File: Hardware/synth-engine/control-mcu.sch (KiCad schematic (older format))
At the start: 31 parts

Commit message: add 3.3V analog regulator and add power nets to AK4490
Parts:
- removed J?: SWD_programming, symbol Connector:Conn_01x05_Male
- removed J? (x2): MIDI IN, symbol Connector:Conn_01x02_Female
- added C? (x7): C_Small, symbol Device:C_Small
- added J?: MIDI_IN, symbol Connector_Generic:Conn_01x02
- added J?: MIDI_OUT, symbol Connector_Generic:Conn_01x02
- added J?: SWD_programming, symbol Connector_Generic:Conn_01x05
- added R? (x14): 0, symbol Device:R
- added RV? (x7): 20kB, symbol Device:R_POT
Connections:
- net labels added: 3.3V, GND, attack, decay, lfo_depth, lfo_rate, release, sustain, waveshape
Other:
- note added: "Envelope Control Pots (ADSR)"
- note added: "LFO"
- note added: "MIDI"
- note added: "Waveshape"
- moved on the sheet: D?, Q?, R?, U?

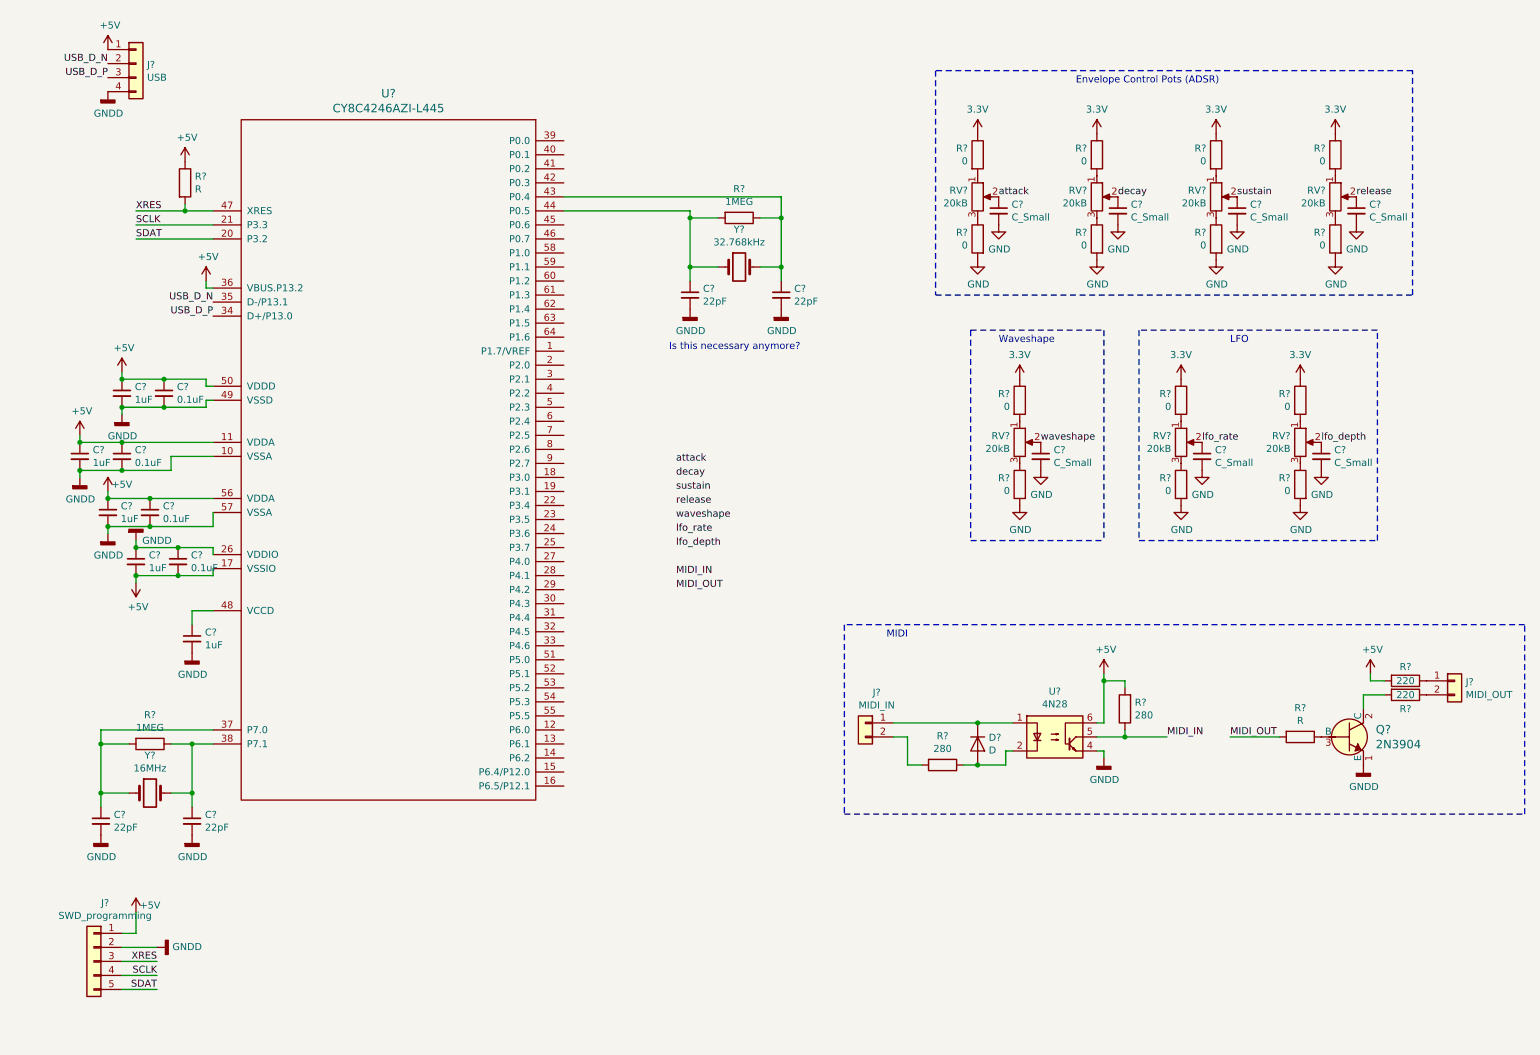
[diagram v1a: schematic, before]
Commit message: add potentiometers for 2 oscillators * I Think this will be all I need for potentiometers   * Until I think of something else to add, of course. * Waveshape will be a continuous change through all of the waves * Tune will be a center frequency control   * Basically just an offset away from the MIDI note's frequency
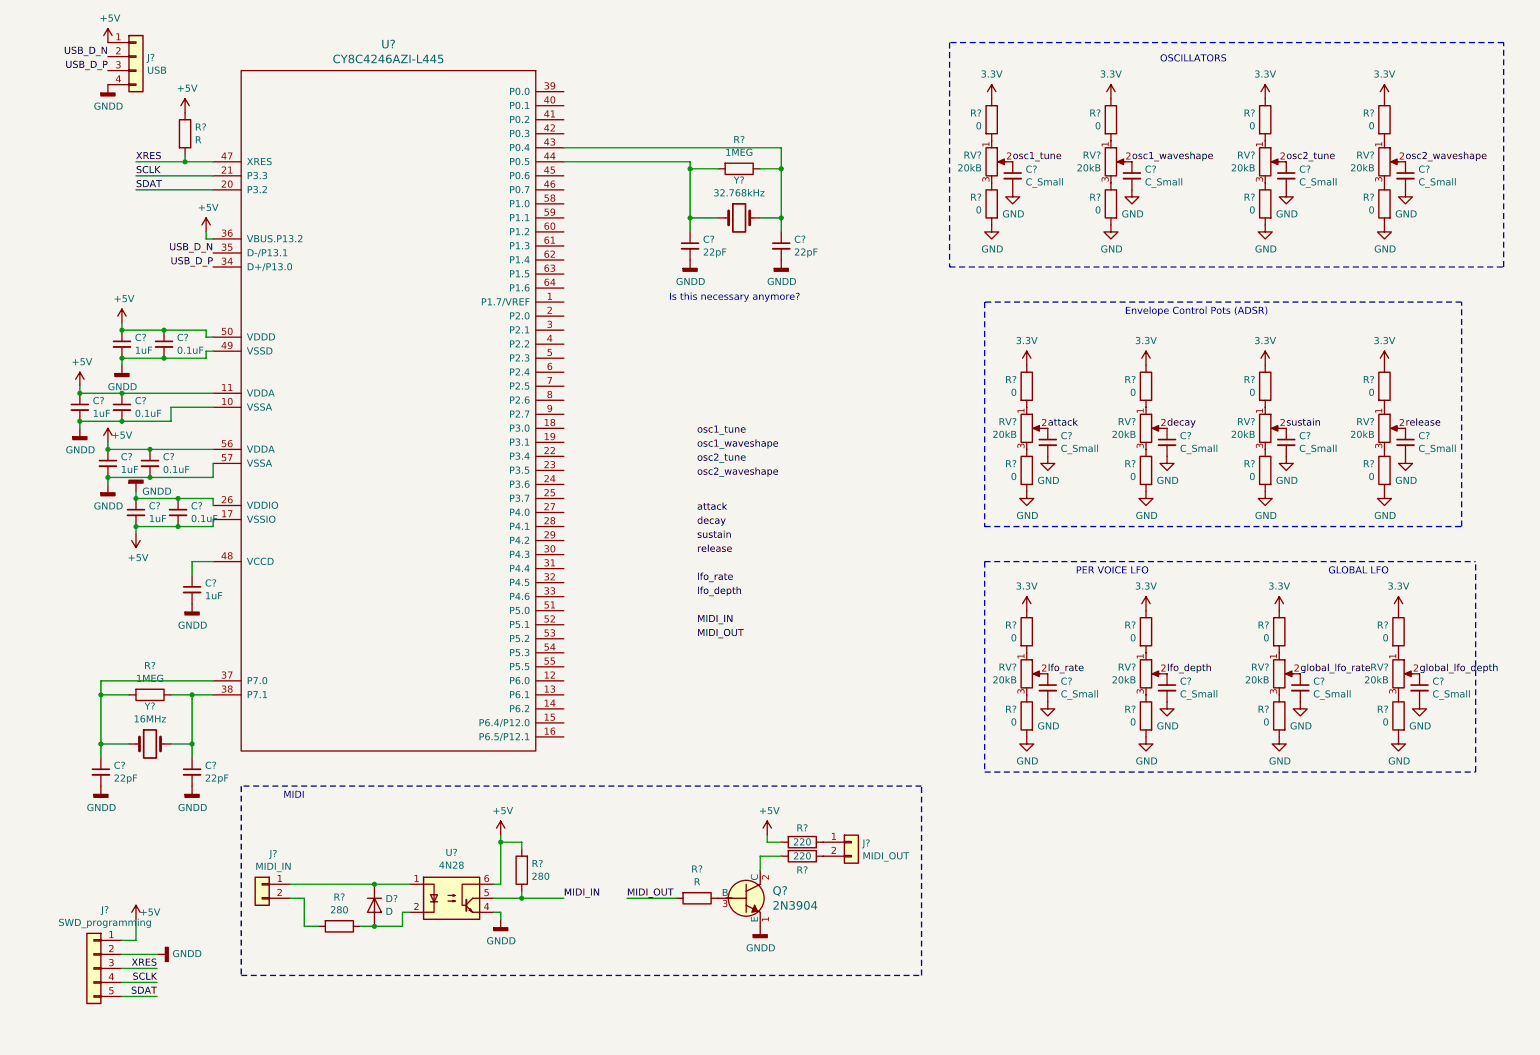
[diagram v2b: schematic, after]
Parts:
- added C? (x5): C_Small, symbol Device:C_Small
- added R? (x10): 0, symbol Device:R
- added RV? (x5): 20kB, symbol Device:R_POT
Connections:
- net 3.3V: now also R?.1, R?.1, R?.1, R?.1, R?.1
- net GND: now also C?.2, C?.2, C?.2, C?.2, C?.2, R?.2, R?.2, R?.2, R?.2, R?.2
- net lfo_depth: now also C?.1, RV?.2; no longer C?.1, RV?.2
- net lfo_rate: now also C?.1, RV?.2; no longer C?.1, RV?.2
- net waveshape renamed osc1_tune
- new net: R?.2, RV?.1 (x5)
- new net: R?.1, RV?.3 (x5)
- new net global_lfo_depth: C?.1, RV?.2
- new net global_lfo_rate: C?.1, RV?.2
- new net osc1_waveshape: C?.1, RV?.2
- new net osc2_tune: C?.1, RV?.2
- new net osc2_waveshape: C?.1, RV?.2
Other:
- note added: "GLOBAL LFO"
- note added: "OSCILLATORS"
- note added: "PER VOICE LFO"
- note removed: "LFO"
- note removed: "Waveshape"
- moved on the sheet: C?, D?, J?, Q?, R?, RV?, U?, Y?

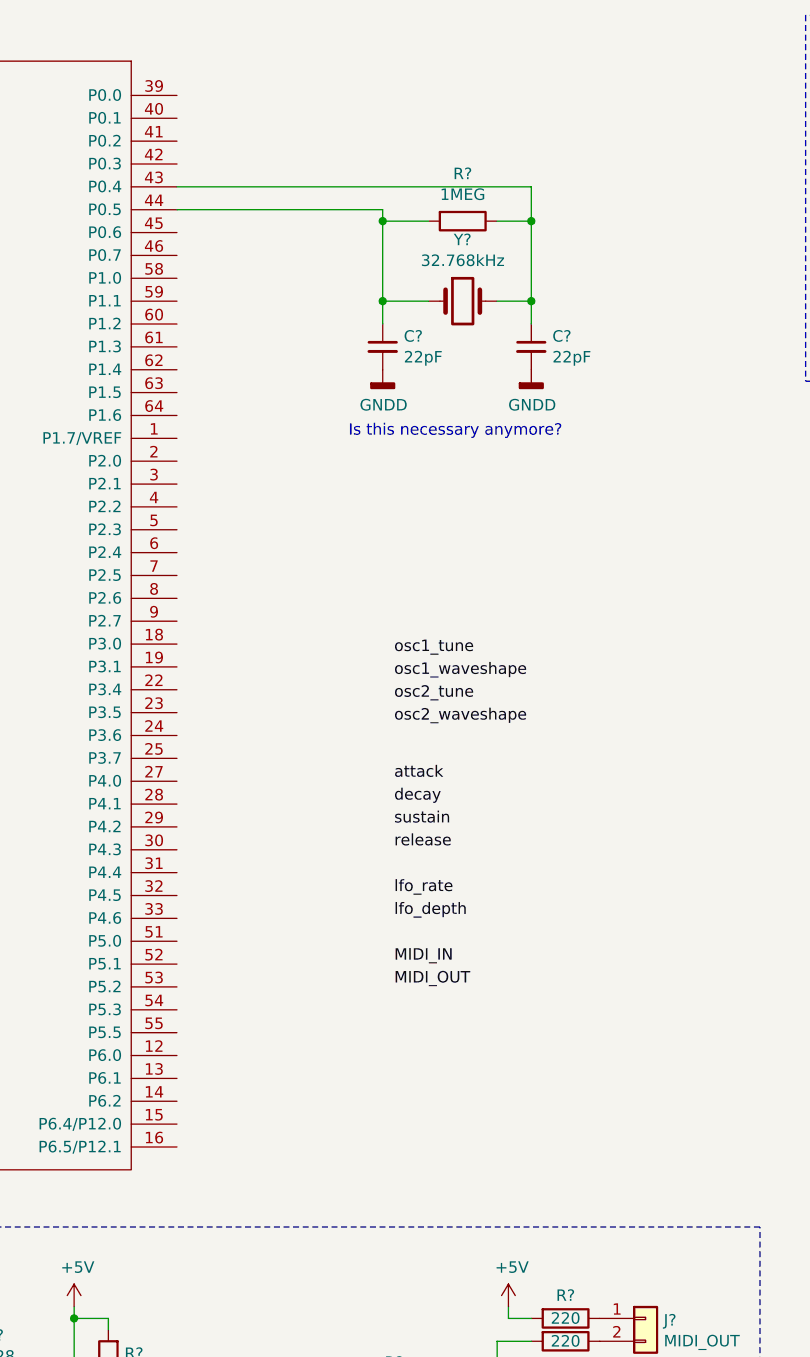
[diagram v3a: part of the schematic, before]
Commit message: delete low frequency crystal on PSoC schematic
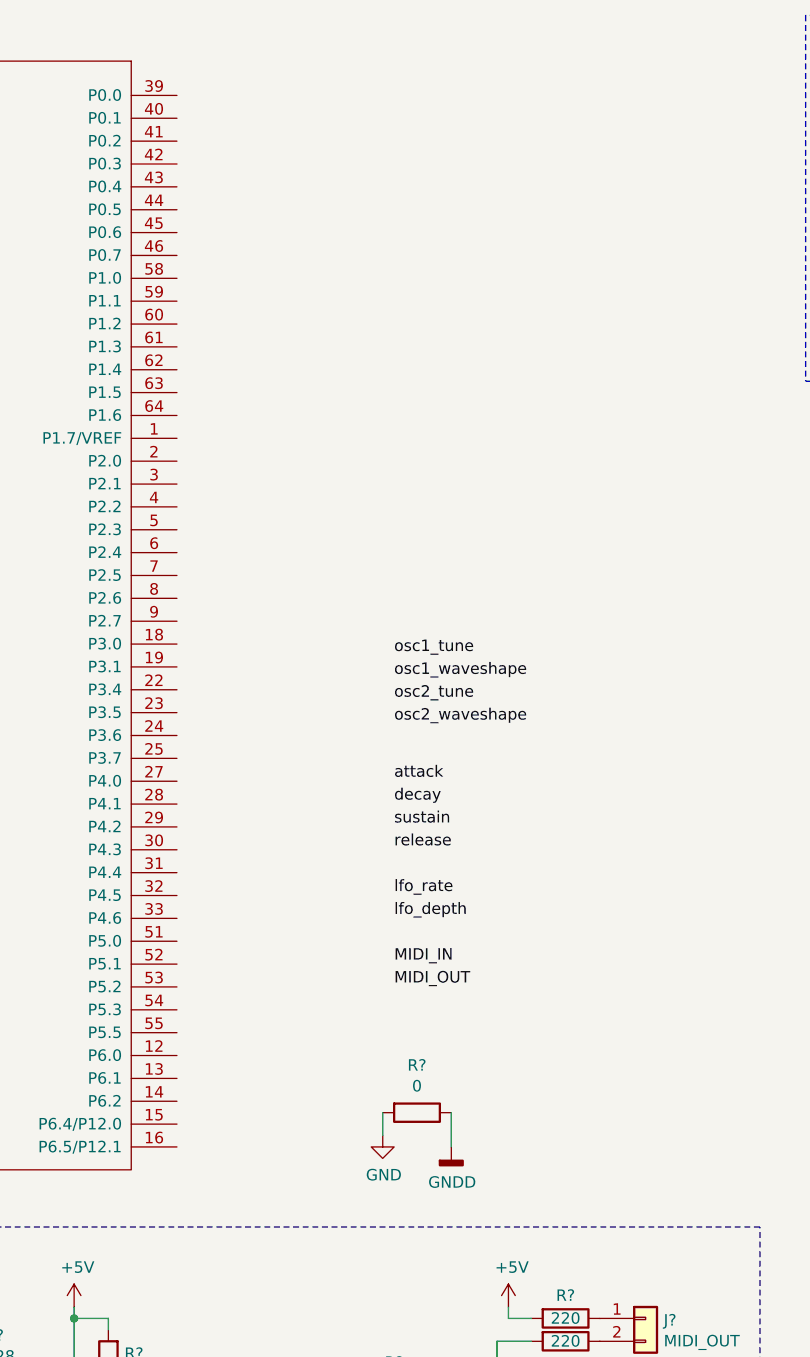
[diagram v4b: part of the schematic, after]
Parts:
- removed C? (x2): 22pF, symbol Device:C_Small
- removed R?: 1MEG, symbol Device:R
- removed Y?: 32.768kHz, symbol Device:Crystal
- added R?: 0, symbol Device:R
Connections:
- net GND: now also R?.2
- net GNDD: now also R?.1
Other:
- note removed: "Is this necessary anymore?"
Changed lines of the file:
@@
 Text Label 5050 3850 0    50   ~ 0
 osc2_waveshape
-Text Notes 4850 2600 0    50   ~ 0
-Is this necessary anymore?
-Wire Wire Line
-	4100 1600 5000 1600
-Wire Wire Line
-	4100 1500 5650 1500
-Wire Wire Line
-	5000 2000 5000 2100
-Connection ~ 5000 2000
-Wire Wire Line
-	5200 2000 5000 2000
 $Comp
-L power:GNDD #PWR?
-U 1 1 5DDBF7A4
-P 5650 2300
-F 0 "#PWR?" H 5650 2050 50  0001 C CNN
-F 1 "GNDD" H 5654 2145 50  0000 C CNN
-F 2 "" H 5650 2300 50  0001 C CNN
-F 3 "" H 5650 2300 50  0001 C CNN
-	1    5650 2300
-	1    0    0    -1
-$EndComp
-$Comp
-L power:GNDD #PWR?
-U 1 1 5DDBF79E
-P 5000 2300
-F 0 "#PWR?" H 5000 2050 50  0001 C CNN
-F 1 "GNDD" H 5004 2145 50  0000 C CNN
-F 2 "" H 5000 2300 50  0001 C CNN
-F 3 "" H 5000 2300 50  0001 C CNN
-	1    5000 2300
-	1    0    0    -1
-$EndComp
-Wire Wire Line
-	5000 1600 5000 1650
-Wire Wire Line
-	5000 1650 5000 2000
-Connection ~ 5000 1650
-Wire Wire Line
-	5200 1650 5000 1650
-Wire Wire Line
-	5500 2000 5650 2000
-Wire Wire Line
-	5650 1500 5650 1650
-Wire Wire Line
-	5650 2000 5650 1650
-Connection ~ 5650 1650
-Wire Wire Line
-	5650 1650 5500 1650
-Connection ~ 5650 2000
-Wire Wire Line
-	5650 2100 5650 2000
-$Comp
-L Device:Crystal Y?
-U 1 1 5DDBF790
-P 5350 2000
-F 0 "Y?" H 5350 2268 50  0000 C CNN
-F 1 "32.768kHz" H 5350 2177 50  0000 C CNN
-F 2 "" H 5350 2000 50  0001 C CNN
-F 3 "~" H 5350 2000 50  0001 C CNN
-	1    5350 2000
-	1    0    0    -1
-$EndComp
-$Comp
-L Device:C_Small C?
-U 1 1 5DDBF789
-P 5650 2200
-F 0 "C?" H 5742 2246 50  0000 L CNN
-F 1 "22pF" H 5742 2155 50  0000 L CNN
-F 2 "" H 5650 2200 50  0001 C CNN
-F 3 "~" H 5650 2200 50  0001 C CNN
-	1    5650 2200
-	1    0    0    -1
-$EndComp
-$Comp
-L Device:C_Small C?
-U 1 1 5DDBF782
-P 5000 2200
-F 0 "C?" H 5092 2246 50  0000 L CNN
-F 1 "22pF" H 5092 2155 50  0000 L CNN
-F 2 "" H 5000 2200 50  0001 C CNN
-F 3 "~" H 5000 2200 50  0001 C CNN
-	1    5000 2200
+L power:GND #PWR?
+U 1 1 5DD70135
+P 5000 5650
+F 0 "#PWR?" H 5000 5400 50  0001 C CNN
+F 1 "GND" H 5005 5477 50  0000 C CNN
+F 2 "" H 5000 5650 50  0001 C CNN
+F 3 "" H 5000 5650 50  0001 C CNN
+	1    5000 5650
 	1    0    0    -1
 $EndComp
 $Comp
 L Device:R R?
-U 1 1 5DDBF77B
-P 5350 1650
-F 0 "R?" V 5143 1650 50  0000 C CNN
-F 1 "1MEG" V 5234 1650 50  0000 C CNN
-F 2 "" V 5280 1650 50  0001 C CNN
-F 3 "~" H 5350 1650 50  0001 C CNN
-	1    5350 1650
+U 1 1 5DD70259
+P 5150 5550
+F 0 "R?" V 4943 5550 50  0000 C CNN
+F 1 "0" V 5034 5550 50  0000 C CNN
+F 2 "" V 5080 5550 50  0001 C CNN
+F 3 "~" H 5150 5550 50  0001 C CNN
+	1    5150 5550
 	0    1    1    0
 $EndComp
+Wire Wire Line
+	5000 5550 5000 5650
+$Comp
+L power:GNDD #PWR?
+U 1 1 5DD74B76
+P 5300 5700
+F 0 "#PWR?" H 5300 5450 50  0001 C CNN
+F 1 "GNDD" H 5304 5545 50  0000 C CNN
+F 2 "" H 5300 5700 50  0001 C CNN
+F 3 "" H 5300 5700 50  0001 C CNN
+	1    5300 5700
+	1    0    0    -1
+$EndComp
+Wire Wire Line
+	5300 5700 5300 5550
 $EndSCHEMATC

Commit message: add pullup resistors to I2C lines
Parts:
- R?: value R -> 10k
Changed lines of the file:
@@
 P 1400 1400
 F 0 "R?" H 1470 1446 50  0000 L CNN
-F 1 "R" H 1470 1355 50  0000 L CNN
+F 1 "10k" H 1470 1355 50  0000 L CNN
 F 2 "" V 1330 1400 50  0001 C CNN
 F 3 "~" H 1400 1400 50  0001 C CNN

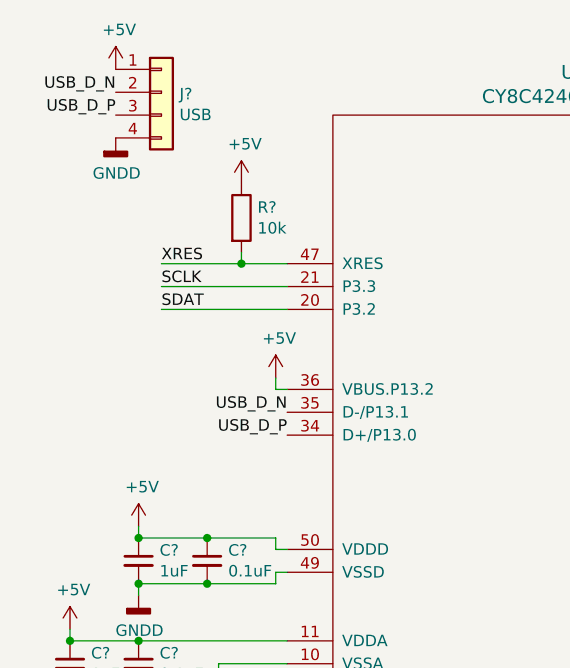
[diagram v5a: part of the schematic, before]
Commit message: clean up USB connector No need to connect this to anything other than PSoC
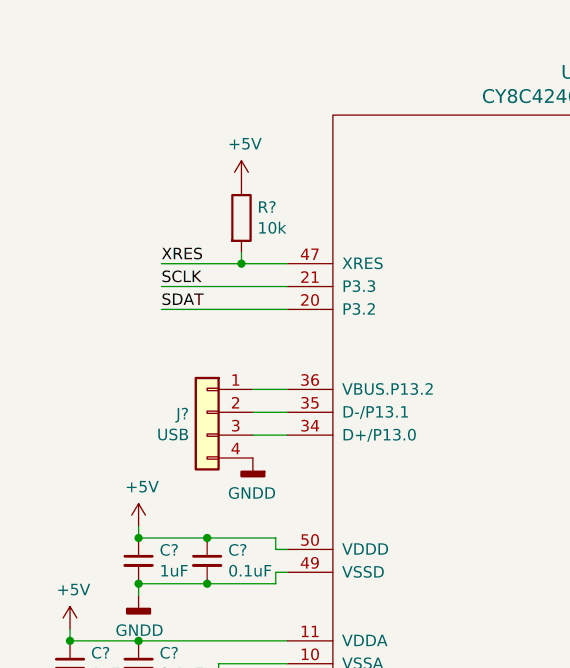
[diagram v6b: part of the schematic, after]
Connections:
- net +5V: no longer J?.1 (Pin_1), U?.36 (VBUS.P13.2)
- net USB_D_N: no longer names the net of J?.2 (Pin_2), U?.35 (D-/P13.1)
- net USB_D_P: no longer names the net of J?.3 (Pin_3), U?.34 (D+/P13.0)
- new net: J?.1 (Pin_1), U?.36 (VBUS.P13.2)
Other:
- moved on the sheet: J?
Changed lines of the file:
@@
-$Comp
-L power:+5V #PWR?
-U 1 1 5DDBF5F3
-P 1550 2100
-F 0 "#PWR?" H 1550 1950 50  0001 C CNN
-F 1 "+5V" H 1565 2273 50  0000 C CNN
-F 2 "" H 1550 2100 50  0001 C CNN
-F 3 "" H 1550 2100 50  0001 C CNN
-	1    1550 2100
-	1    0    0    -1
-$EndComp
-Wire Wire Line
-	1550 2100 1550 2150
-Wire Wire Line
-	1550 2150 1600 2150
 $Comp
 L power:+5V #PWR?
@@
 L Connector_Generic:Conn_01x04 J?
 U 1 1 5DDBF7B4
-P 1050 850
-F 0 "J?" H 1129 842 50  0000 L CNN
-F 1 "USB" H 1129 751 50  0000 L CNN
-F 2 "" H 1050 850 50  0001 C CNN
-F 3 "~" H 1050 850 50  0001 C CNN
-	1    1050 850
-	1    0    0    -1
-$EndComp
-$Comp
-L power:+5V #PWR?
-U 1 1 5DDBF7BB
-P 850 750
-F 0 "#PWR?" H 850 600 50  0001 C CNN
-F 1 "+5V" H 865 923 50  0000 C CNN
-F 2 "" H 850 750 50  0001 C CNN
-F 3 "" H 850 750 50  0001 C CNN
-	1    850  750
-	1    0    0    -1
+P 1250 2250
+F 0 "J?" H 1329 2242 50  0000 L CNN
+F 1 "USB" H 1329 2151 50  0000 L CNN
+F 2 "" H 1250 2250 50  0001 C CNN
+F 3 "~" H 1250 2250 50  0001 C CNN
+	1    1250 2250
+	-1   0    0    -1
 $EndComp
 $Comp
 L power:GNDD #PWR?
 U 1 1 5DDBF7C1
-P 850 1050
-F 0 "#PWR?" H 850 800 50  0001 C CNN
-F 1 "GNDD" H 854 895 50  0000 C CNN
-F 2 "" H 850 1050 50  0001 C CNN
-F 3 "" H 850 1050 50  0001 C CNN
-	1    850  1050
-	1    0    0    -1
-$EndComp
-Text Label 850  850  2    50   ~ 0
-USB_D_N
-Text Label 850  950  2    50   ~ 0
-USB_D_P
-Text Label 1600 2250 2    50   ~ 0
-USB_D_N
-Text Label 1600 2350 2    50   ~ 0
-USB_D_P
+P 1450 2450
+F 0 "#PWR?" H 1450 2200 50  0001 C CNN
+F 1 "GNDD" H 1454 2295 50  0000 C CNN
+F 2 "" H 1450 2450 50  0001 C CNN
+F 3 "" H 1450 2450 50  0001 C CNN
+	1    1450 2450
+	-1   0    0    -1
+$EndComp
 $Comp
 L SparkFun-Aesthetics:3.3V #SUPPLY?
@@
 Wire Wire Line
 	5300 5700 5300 5550
+Wire Wire Line
+	1600 2150 1450 2150
+Wire Wire Line
+	1450 2250 1600 2250
+Wire Wire Line
+	1600 2350 1450 2350
 $EndSCHEMATC
